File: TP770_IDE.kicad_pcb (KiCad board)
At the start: 2 copper layers, 71 x 53 mm, 3 parts, among them J1 CF Card, J2 TP770IDE

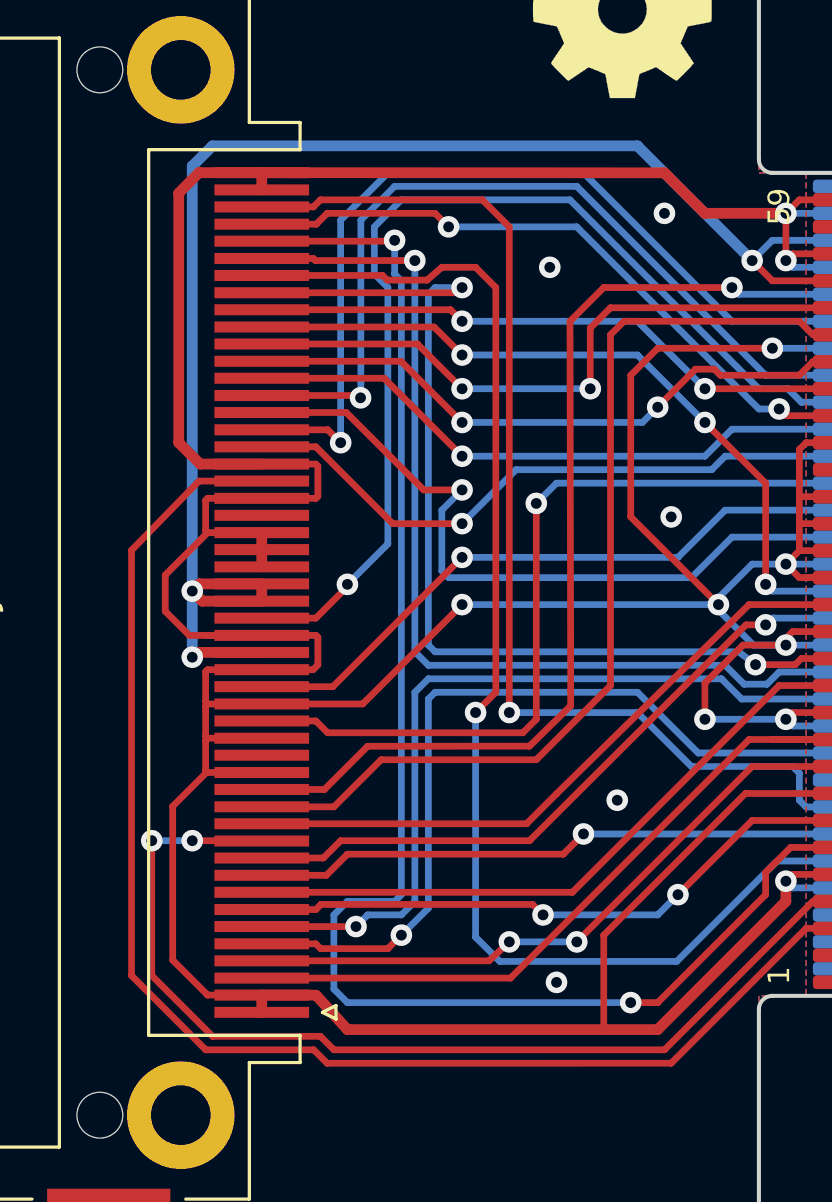
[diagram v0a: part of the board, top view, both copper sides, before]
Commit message: Improved copper pours
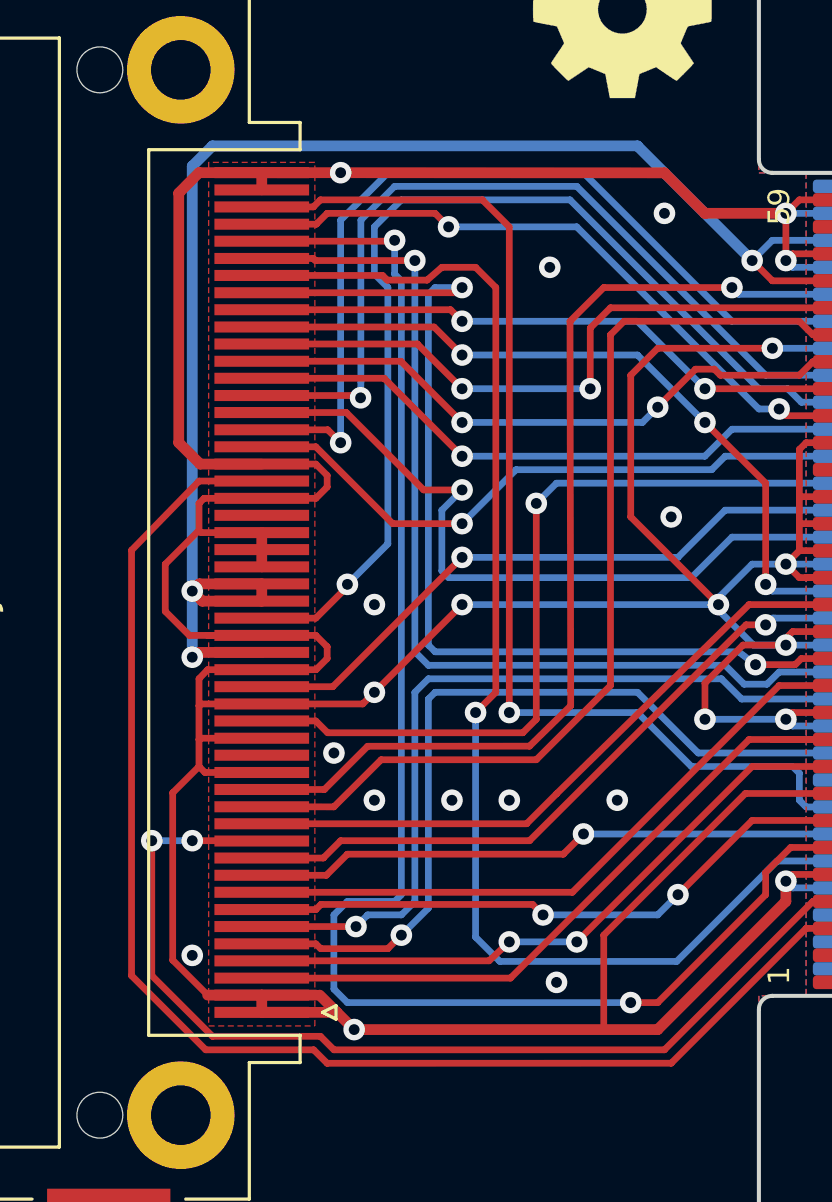
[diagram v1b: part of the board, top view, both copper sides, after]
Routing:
- net GND: track 243.0 -> 247.7 mm, vias 15 -> 24

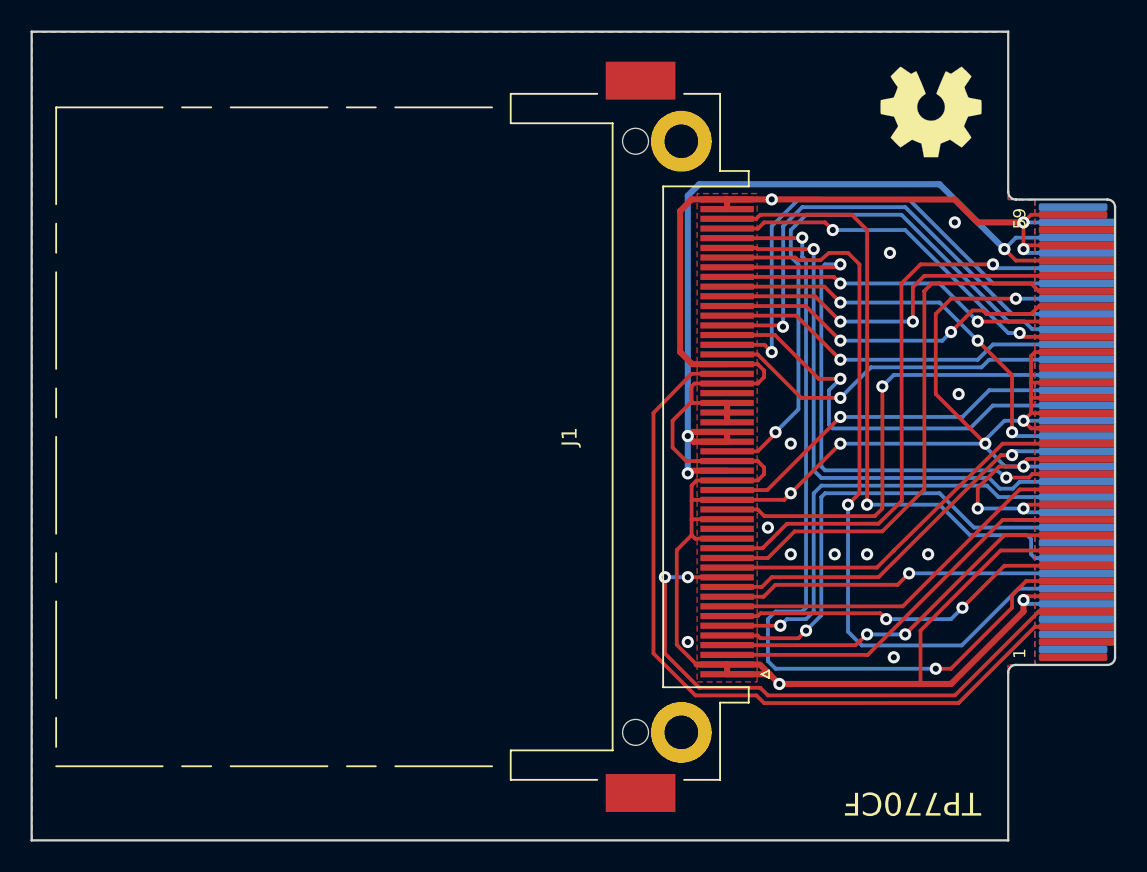
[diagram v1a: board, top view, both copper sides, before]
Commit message: Upgraded to KiCAD 6.0 Cleaned & passing DRC Added Gerbers & drill files Added revision code
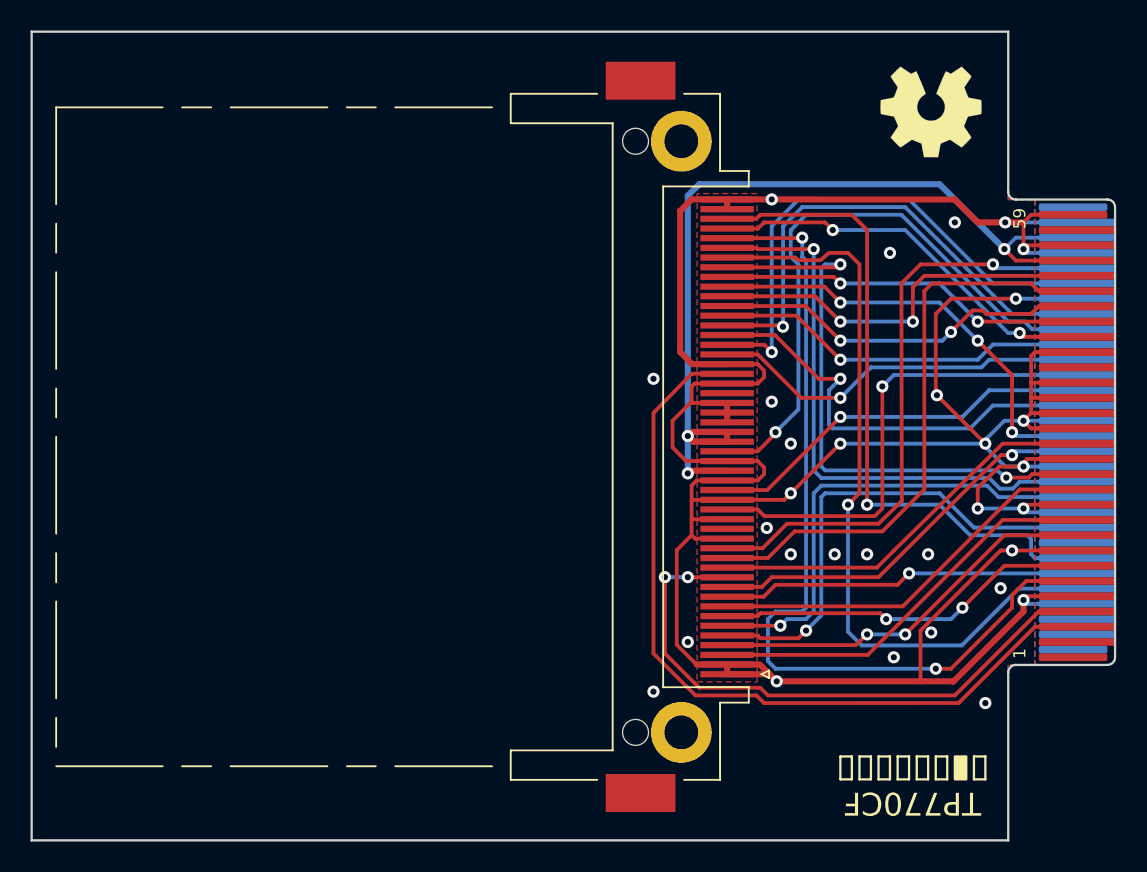
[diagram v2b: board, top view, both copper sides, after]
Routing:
- net Net-(J1-Pad2): track 30.6 -> 26.6 mm
- net GND: track 247.7 -> 248.6 mm, vias 24 -> 31
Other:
- net class Default removed
- rule pad_to_mask_clearance: 0.051 -> 0
